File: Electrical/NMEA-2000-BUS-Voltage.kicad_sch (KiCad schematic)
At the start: 13 parts, among them K2 RAYEX-L90, U1 ACS712-Module, U2 LM7805_TO220, U3 SN65HVD230-Module, U4 BMP280-Module

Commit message: Updated Schematics
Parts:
- removed A1: Adafruit_Feather_HUZZAH32_ESP32, Module:Adafruit_Feather, symbol MCU_Module:Adafruit_Feather_HUZZAH32_ESP32
- removed K2: RAYEX-L90, Relay_THT:Relay_SPDT_RAYEX-L90, symbol Relay:RAYEX-L90
- removed U1: ACS712-Module, symbol ACS712:ACS712-Module
- removed U3: SN65HVD230-Module, symbol sn65hvd230-module:SN65HVD230-Module
- added C4: 0.33uF, Capacitor_THT:C_Disc_D3.0mm_W1.6mm_P2.50mm, symbol Device:C_Small
- added C5: 680uF, Capacitor_THT:C_Disc_D3.0mm_W1.6mm_P2.50mm, symbol Device:C_Polarized
- added D1: 1N5821, Diode_THT:D_DO-201_P15.24mm_Horizontal, symbol Device:D_Schottky_Small
- added J1: Conn_01x04, TerminalBlock_Phoenix:TerminalBlock_Phoenix_MKDS-1,5-4-5.08_1x04_P5.08mm_Horizontal, symbol Connector_Generic:Conn_01x04
- added J2: Conn_01x04, Connector_PinSocket_2.54mm:PinSocket_1x04_P2.54mm_Horizontal, symbol Connector_Generic:Conn_01x04
- added J3: Conn_01x02, symbol Connector_Generic:Conn_01x02
- added J4: Conn_01x03, Connector_Phoenix_MC:PhoenixContact_MC_1,5_3-G-3.81_1x03_P3.81mm_Horizontal, symbol Connector_Generic:Conn_01x03
- added L1: 100uH, Inductor_THT:L_Radial_D6.0mm_P4.00mm, symbol Device:L
- added Q1: IRFZ44N, Package_TO_SOT_THT:TO-220-3_Vertical, symbol Simulation_SPICE:NMOS
- added R1, R2: 10k, Resistor_THT:R_Axial_DIN0204_L3.6mm_D1.6mm_P5.08mm_Horizontal, symbol Device:R
- added R3: 2.2k, Resistor_THT:R_Axial_DIN0204_L3.6mm_D1.6mm_P5.08mm_Horizontal, symbol Device:R_Small
- added R4: 17.4k, Resistor_THT:R_Axial_DIN0204_L3.6mm_D1.6mm_P5.08mm_Horizontal, symbol Device:R_Small
- added R5: 2k, Resistor_THT:R_Axial_DIN0204_L3.6mm_D1.6mm_P5.08mm_Horizontal, symbol Device:R_Small
- added R6: R, Resistor_THT:R_Axial_DIN0204_L3.6mm_D1.6mm_P5.08mm_Horizontal, symbol Device:R
- added U2: ESP32_NODEMCU, esp32:esp32, symbol ESP32_NODEMCU:ESP32_NODEMCU
- added U3: LM2577T-ADJ_NOPB, Libraries:VREG_LM2577T-ADJ_NOPB, symbol LM2577T-ADJ_NOPB:LM2577T-ADJ_NOPB
- added U5: SN65HVD230, Package_SO:SOIC-8_3.9x4.9mm_P1.27mm, symbol Interface_CAN_LIN:SN65HVD230
- C1, C2, C3: footprint (none) -> Capacitor_THT:C_Disc_D3.0mm_W1.6mm_P2.50mm
- R10: renamed from R4; footprint (none) -> Resistor_THT:R_Axial_DIN0204_L3.6mm_D1.6mm_P5.08mm_Horizontal
- R7: renamed from R1; footprint (none) -> Resistor_THT:R_Axial_DIN0204_L3.6mm_D1.6mm_P5.08mm_Horizontal
- R8: renamed from R2; footprint (none) -> Resistor_THT:R_Axial_DIN0204_L3.6mm_D1.6mm_P5.08mm_Horizontal
- R9: renamed from R3; footprint (none) -> Resistor_THT:R_Axial_DIN0204_L3.6mm_D1.6mm_P5.08mm_Horizontal
- renumbered U2 to U1
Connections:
- net -12V is gone; now on net +12V: C1.1, C2.1, R7.1, U1.1 (VI)
- net +12V: now also J1.1 (Pin_1), L1.1, Q1.1 (D), U3.5 (VIN)
- net +3V3: now also U2.19 (3V3)
- net +5V: now also J2.1 (Pin_1), U2.1 (5V)
- net A0: now also U2.8 (G14)
- net A1: now also U2.23 (G15)
- net CAN_H: now also J1.3 (Pin_3), U5.7 (CANH)
- net CAN_L: now also J1.2 (Pin_2), U5.6 (CANL)
- net C_RX: now also U2.30 (G18)
- net C_TX: now also U2.28 (G17)
- net GND: now also C4.2, C5.2, J1.4 (Pin_4), J2.4 (Pin_4), J3.2 (Pin_2), J4.3 (Pin_3), R2.2, R5.2, U2.32 (GND_J4_7), U2.38 (GND_J5_6), U2.6 (GND_J4_1), U3.3 (GROUND), U5.2 (GND)
- net IO15: now also Q1.2 (G), U2.27 (G16)
- net MISO: now also U2.7 (G12)
- net MOSI: now also U2.5 (G13)
- net RX: now also J2.2 (Pin_2), U2.34 (RXD)
- net SCK: now also U2.29 (G5)
- net SCL: now also U2.26 (G4)
- net SDA: now also U2.24 (G2)
- net TX: now also J2.3 (Pin_3), U2.35 (TXD)
- new net: R6.2, U5.8 (Rs)
- new net: J4.2 (Pin_2), R1.1
- new net: R4.2, R5.1, U3.2 (FEEDBACK)
- new net: R3.1, U3.1 (COMP)
- new net: D1.2 (A), L1.2, U3.4 (SWITCH)
- new net: C4.1, R3.2
- new net +15V: C5.1, D1.1 (K), J4.1 (Pin_1), R4.1
- new net +3.3V: R6.1, U5.3 (VCC)
- new net CAN_RX: U5.1 (D)
- new net CAN_TX: U5.4 (R)
- new net CON: J3.1 (Pin_1), Q1.3 (S)
- new net CUR: R1.2, R2.1, U2.31 (G19)
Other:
- moved on the sheet: C1, C2, C3, R10, R7, R8, R9, U1, U4

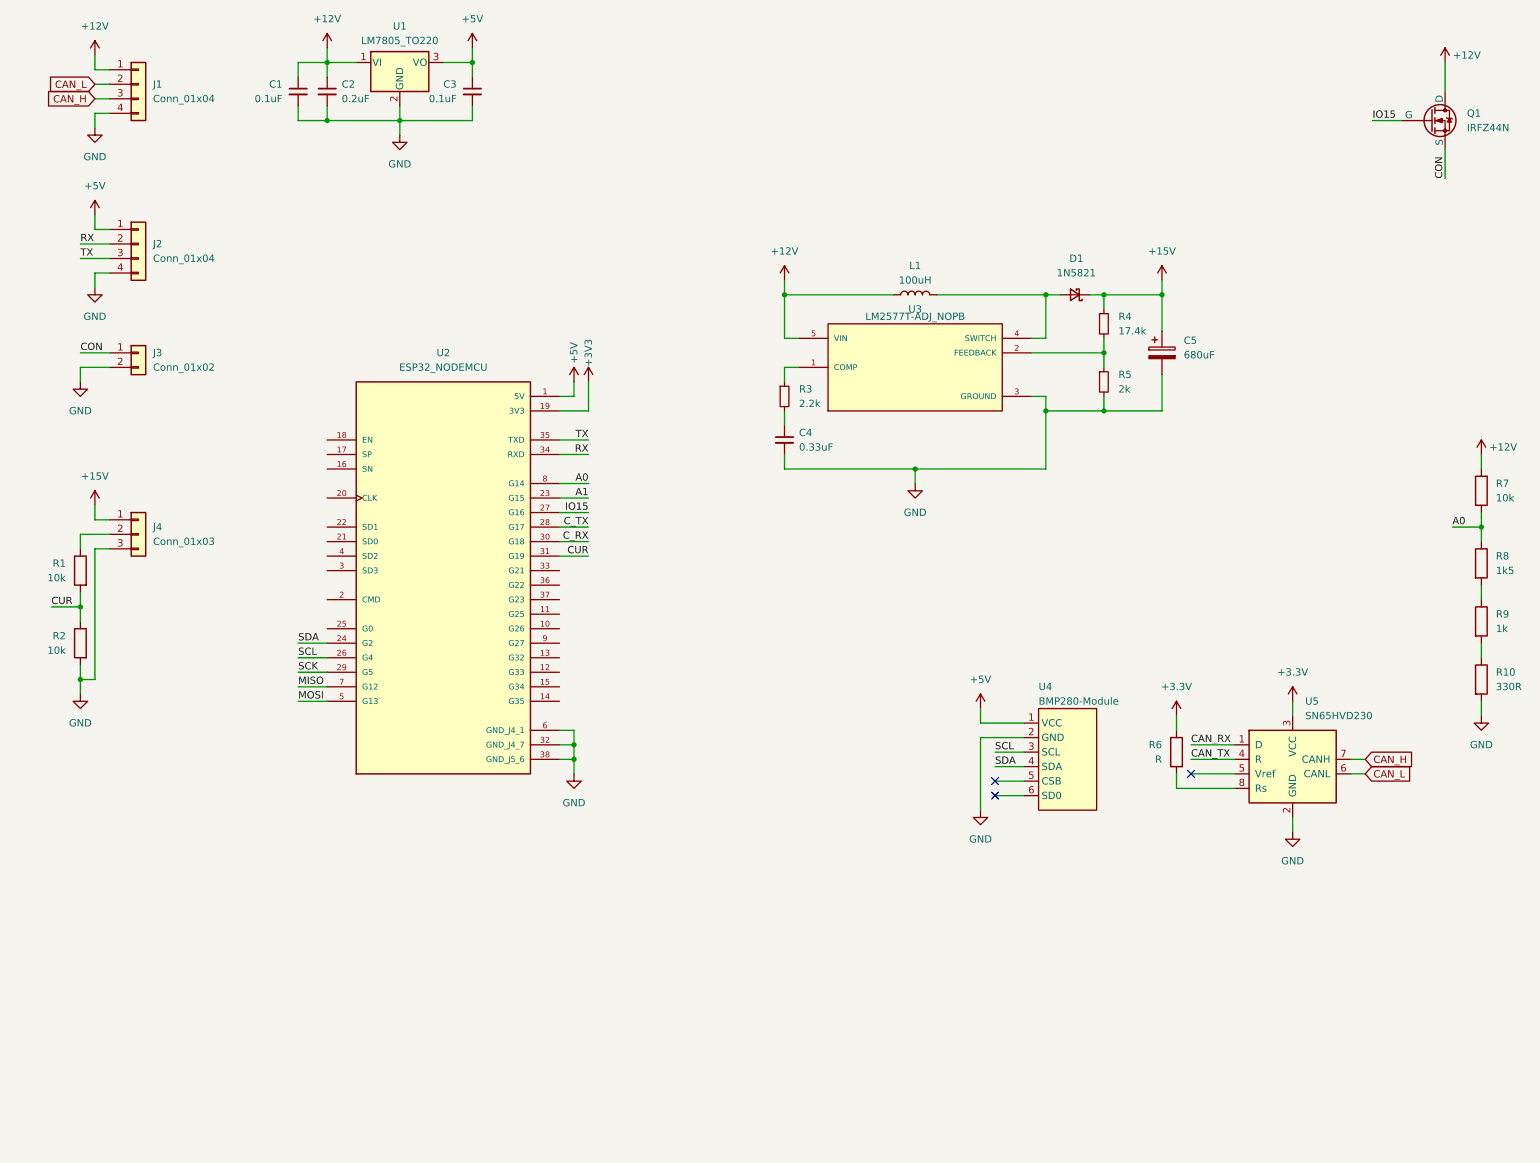
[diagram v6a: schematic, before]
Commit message: Added PWM Fan control
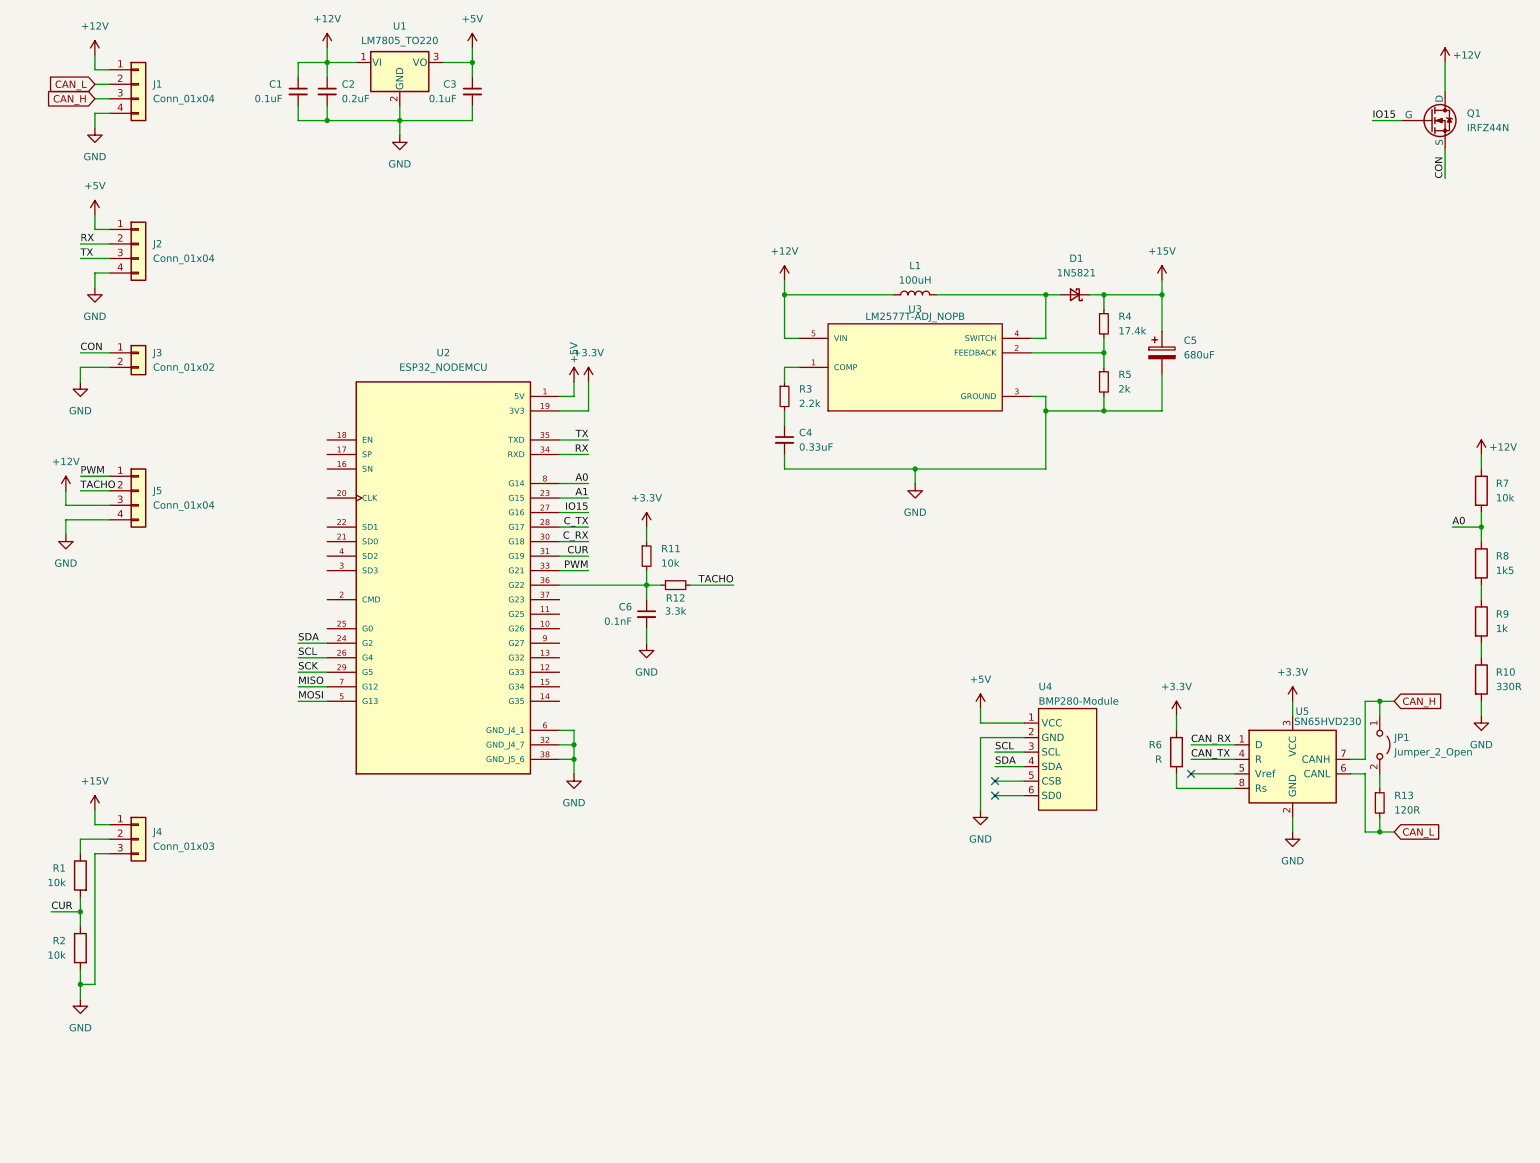
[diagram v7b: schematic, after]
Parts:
- added C6: 0.1nF, Connector_PinHeader_2.54mm:PinHeader_1x02_P2.54mm_Vertical, symbol Device:C_Small
- added J5: Conn_01x04, Connector:FanPinHeader_1x04_P2.54mm_Vertical, symbol Connector_Generic:Conn_01x04
- added JP1: Jumper_2_Open, Connector_PinHeader_2.54mm:PinHeader_1x02_P2.54mm_Vertical, symbol Jumper:Jumper_2_Open
- added R11: 10k, Resistor_THT:R_Axial_DIN0204_L3.6mm_D1.6mm_P5.08mm_Horizontal, symbol Device:R_Small
- added R12: 3.3k, Resistor_THT:R_Axial_DIN0204_L3.6mm_D1.6mm_P5.08mm_Horizontal, symbol Device:R_Small
- added R13: 120R, Resistor_THT:R_Axial_DIN0204_L3.6mm_D1.6mm_P5.08mm_Horizontal, symbol Device:R_Small
- J1: footprint TerminalBlock_Phoenix:TerminalBlock_Phoenix_MKDS-1,5-4-5.08_1x04_P5.08mm_Horizontal -> TerminalBlock_Phoenix:TerminalBlock_Phoenix_PT-1,5-4-5.0-H_1x04_P5.00mm_Horizontal
- J3: footprint (none) -> TerminalBlock_Phoenix:TerminalBlock_Phoenix_PT-1,5-2-5.0-H_1x02_P5.00mm_Horizontal
- U4: footprint (none) -> Connector_PinSocket_2.54mm:PinSocket_1x06_P2.54mm_Horizontal
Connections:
- net +3V3 is gone; now on net +3.3V: U2.19 (3V3)
- net +12V: now also J5.3 (Pin_3)
- net +3.3V: now also R11.1
- net CAN_H: now also JP1.1 (A)
- net CAN_L: now also R13.2
- net GND: now also C6.2, J5.4 (Pin_4)
- net PWM: now reaches U2.33 (G21)
- net PWM: now also J5.1 (Pin_1)
- net at U2.36 (G22): now also C6.1, R11.2, R12.1
- new net: JP1.2 (B), R13.1
- new net TACHO: J5.2 (Pin_2), R12.2
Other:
- moved on the sheet: J4, R1, R2

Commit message: Added Power LEDs & 12V SDC
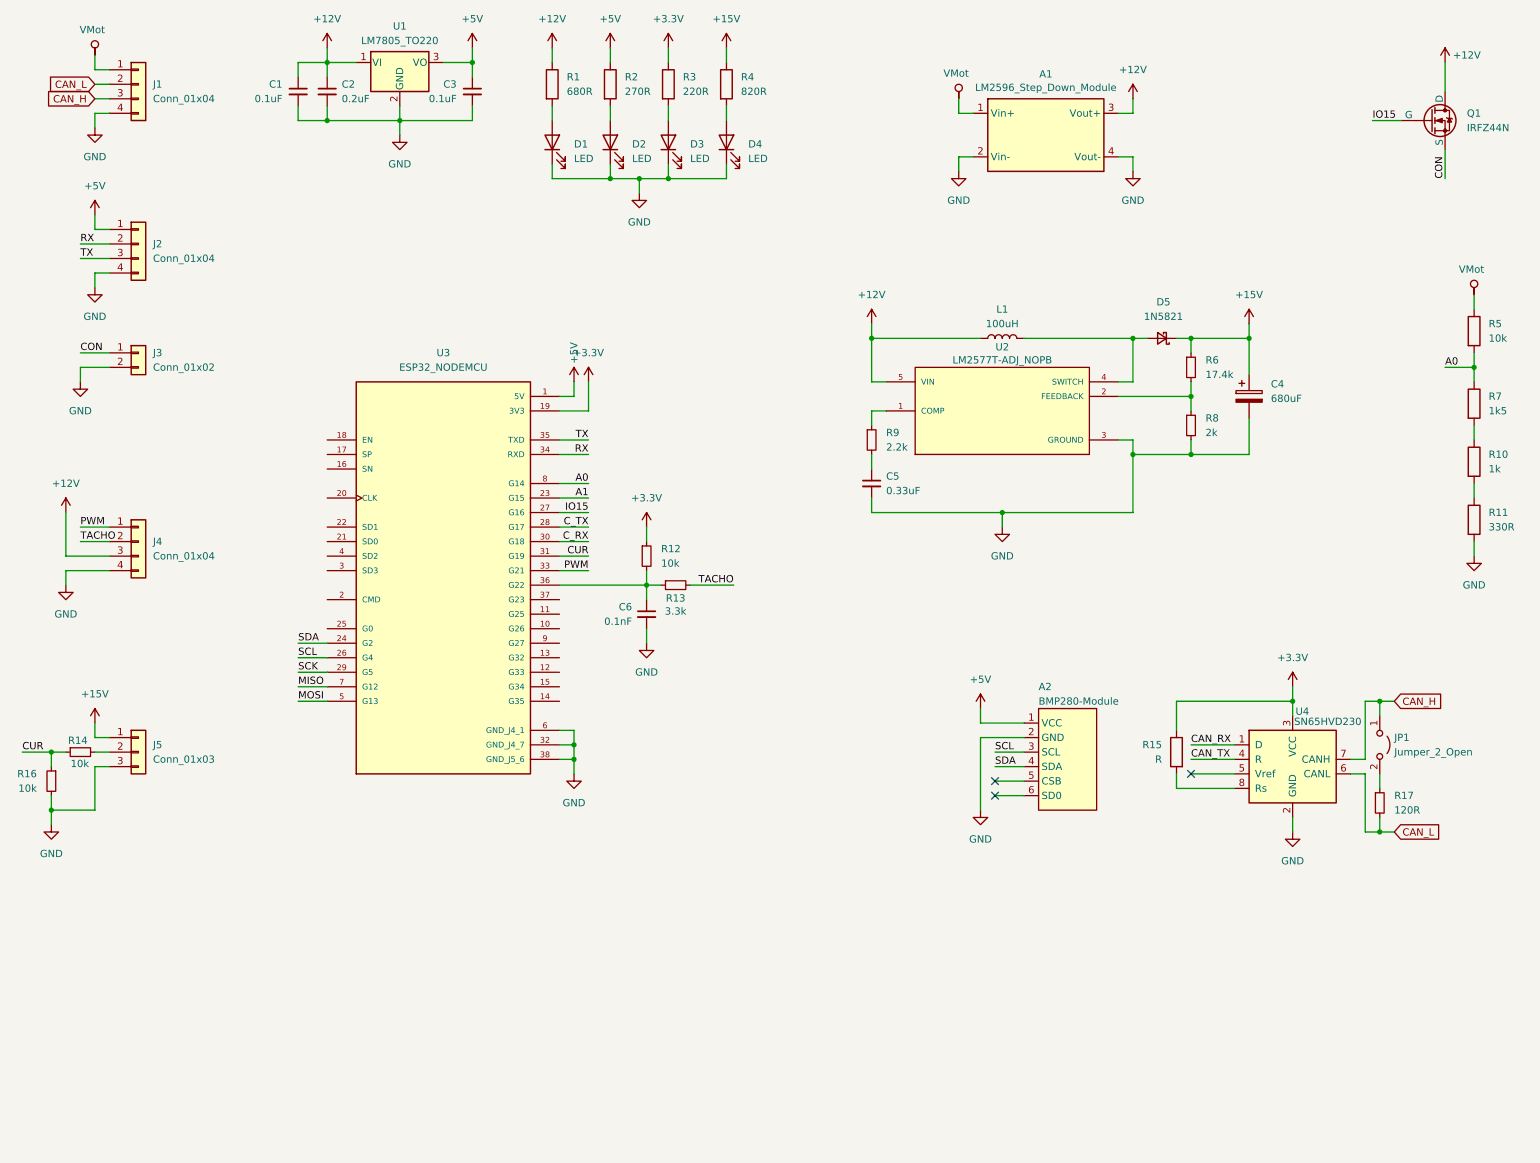
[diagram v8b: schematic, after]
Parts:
- added A1: LM2596_Step_Down_Module, MPCNC_Shield_Footprints:LM2596_Step_Down_Module-21.3x43.6mm, symbol MPCNC_Shield_Symbols:LM2596_Step_Down_Module
- added D1, D2, D3, D4: LED, LED_THT:LED_D5.0mm, symbol Device:LED
- added R1: 680R, Resistor_THT:R_Axial_DIN0204_L3.6mm_D1.6mm_P5.08mm_Horizontal, symbol Device:R
- added R2: 270R, Resistor_THT:R_Axial_DIN0204_L3.6mm_D1.6mm_P5.08mm_Horizontal, symbol Device:R
- added R3: 220R, Resistor_THT:R_Axial_DIN0204_L3.6mm_D1.6mm_P5.08mm_Horizontal, symbol Device:R
- added R4: 820R, Resistor_THT:R_Axial_DIN0204_L3.6mm_D1.6mm_P5.08mm_Horizontal, symbol Device:R
- C4: renamed from C5; footprint Capacitor_THT:C_Disc_D3.0mm_W1.6mm_P2.50mm -> Capacitor_THT:CP_Radial_D8.0mm_P3.50mm
- R14: renamed from R1; symbol Device:R -> Device:R_Small
- R16: renamed from R2; symbol Device:R -> Device:R_Small
- renumbered U4 to A2, C4 to C5, D1 to D5, J5 to J4, J4 to J5, R9 to R10, R10 to R11, R11 to R12, R12 to R13, R6 to R15, R13 to R17, R7 to R5, R4 to R6, R8 to R7, R5 to R8, R3 to R9, U3 to U2, U2 to U3, U5 to U4
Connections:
- net +12V: now also A1.3 (Vout+), R1.1; no longer J1.1 (Pin_1), R5.1
- net +15V: now also R4.1
- net +3.3V: now also R3.1
- net +5V: now also R2.1
- net CUR: now also R14.1; no longer R14.2
- net GND: now also A1.2 (Vin-), A1.4 (Vout-), D1.1 (K), D2.1 (K), D3.1 (K), D4.1 (K)
- net at J5.2 (Pin_2): now also R14.2; no longer R14.1
- new net: D4.2 (A), R4.2
- new net: D2.2 (A), R2.2
- new net: D3.2 (A), R3.2
- new net: D1.2 (A), R1.2
- new net VMot: A1.1 (Vin+), J1.1 (Pin_1), R5.1
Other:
- moved on the sheet: C4, C5, D5, J4, J5, L1, R10, R11, R14, R16, R5, R6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
